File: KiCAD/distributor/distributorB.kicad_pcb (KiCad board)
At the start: 4 copper layers, 235 x 29 mm, 12 parts, among them P1 CONN_02X03, P11 CONN_02X03, P13 CONN_02X03, P15 CONN_02X03, P17 CONN_02X03, P19 CONN_02X03, P21 CONN_02X22, P3 CONN_02X03, P5 CONN_02X03, P7 CONN_02X03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

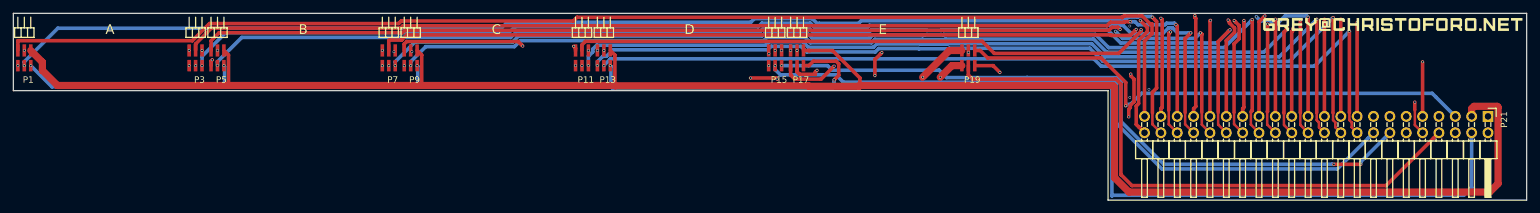
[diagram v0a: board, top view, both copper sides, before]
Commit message: tight spacing 30x30x5 distributor boards done
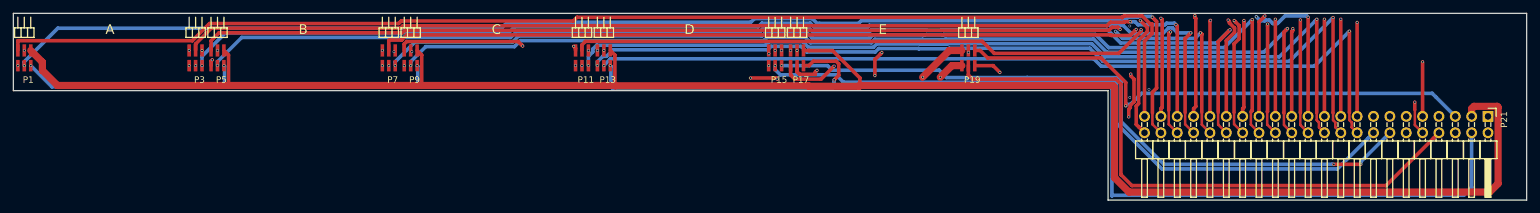
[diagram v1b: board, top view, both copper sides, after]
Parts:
- G***: moved to B.Cu
- turned G*** to 180 degrees
